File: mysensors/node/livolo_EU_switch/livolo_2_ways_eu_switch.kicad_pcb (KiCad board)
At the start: 2 copper layers, 47 parts, among them CON1 AVR-ISP-6, IC1 ATMEGA328P-A, P1 Sense Pad, P2 Sense Pad, P3 ANTENNA, P4 CONN_02X06, U1 MIC5205-3.3, U2 MCP16301, U3 TTP223, U4 TTP223, U5 RFM69HW

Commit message: mysensors livolo EU switch panel schematic/pcb progress - 2nd pass
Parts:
- removed R9: 1K, Resistors_SMD:R_0603_HandSoldering
- added R1: 31K6, Resistors_SMD:R_0603_HandSoldering, F.Cu at (165.0, 106.9)
- CON1: footprint Pin_Headers:Pin_Header_Straight_SMT_02x03 -> myfootprints:AVR_ISP_SMT_Small_02x03
- D3, D6: value LED_Small -> LED_Blue
- D4, D5: value LED_Small -> LED_Red
- P4: value CONN_02X06 -> Power Board
- R2: value 31K6 -> 10K
- R5: value 10K -> 1K
- U5: value RFM69HW -> RFM69CW; footprint mysensors_radios:RFM69HW_SMD_Handsoldering -> myfootprints:RFM69CW
- moved D5 100.4 mm to (145.4, 106.3)
- moved CON1 95.7 mm to (139.8, 91.9)
- moved L2 95.6 mm to (138.2, 105.1)
- moved R8 91.0 mm to (184.6, 103.6)
- moved R6 89.4 mm to (171.0, 105.3)
- moved C12 89.2 mm to (175.5, 105.3)
- moved D3 87.4 mm to (153.9, 106.3)
- moved C1 87.3 mm to (160.4, 106.9)
- moved D6 84.6 mm to (168.5, 93.1)
- moved R5 83.9 mm to (182.0, 93.6)
- moved P1 82.8 mm to (135.1, 76.2)
- moved U1 81.4 mm to (164.7, 86.5)
- moved U3 77.2 mm to (183.2, 80.2)
- moved D2 77.0 mm to (190.1, 79.3)
- moved U5 76.2 mm to (126.1, 96.4)
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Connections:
- net /D0 renamed Net-(IC1-Pad30)
- D3 pad 1: Net-(D3-Pad1) -> GND
- D4 pad 2: Net-(D4-Pad2) -> +3V3
- D5 pad 2: Net-(D5-Pad2) -> +3V3
- D6 pad 1: Net-(D6-Pad1) -> GND
- IC1 pad 12: Net-(IC1-Pad12) -> /S1_LEDs
- IC1 pad 13: Net-(IC1-Pad13) -> /TS1
- IC1 pad 25: Net-(IC1-Pad25) -> /S2_LEDs
- IC1 pad 28: Net-(IC1-Pad28) -> /TS2
- P1 pad 1: Net-(C11-Pad1) -> Net-(C12-Pad1)
- P2 pad 1: Net-(C12-Pad1) -> Net-(C11-Pad1)
- P4 pad 11: Net-(P4-Pad11) -> /12Vcc
- P4 pad 4: Net-(P4-Pad4) -> GND
- R2 pad 1: Net-(R2-Pad1) -> GND
- R2 pad 2: Net-(C7-Pad1) -> Net-(R1-Pad1)
- R3 pad 1: GND -> +3V3
- R3 pad 2: Net-(R2-Pad1) -> /RESET
- R4 pad 1: +3V3 -> /SS
- R4 pad 2: /RESET -> +3V3
- R5 pad 1: /SS -> Net-(D6-Pad2)
- R5 pad 2: +3V3 -> /S1_LEDs
- R6 pad 1: Net-(R6-Pad1) -> Net-(D5-Pad1)
- R6 pad 2: Net-(R6-Pad2) -> /S1_LEDs
- R7 pad 1: Net-(R7-Pad1) -> Net-(D3-Pad2)
- R7 pad 2: Net-(R7-Pad2) -> /S2_LEDs
- R8 pad 1: Net-(R8-Pad1) -> Net-(D4-Pad1)
- R8 pad 2: Net-(R8-Pad2) -> /S2_LEDs
- U2 pad 3: Net-(R2-Pad1) -> Net-(R1-Pad1)
- U3 pad 1: Net-(U3-Pad1) -> /TS1
- U4 pad 1: Net-(U4-Pad1) -> /TS2
- U5 pad 1: Net-(U5-Pad1) -> Net-(P3-Pad1)
- U5 pad 10: Net-(P3-Pad1) -> Net-(U5-Pad10)
- U5 pad 11: GND -> Net-(U5-Pad11)
- U5 pad 12: /SCK -> Net-(U5-Pad12)
- U5 pad 13: /MISO -> Net-(U5-Pad13)
- U5 pad 14: /MOSI -> GND
- U5 pad 2: /INT -> +3V3
- U5 pad 3: Net-(U5-Pad3) -> GND
- U5 pad 5: Net-(U5-Pad5) -> /MOSI
- U5 pad 6: Net-(U5-Pad6) -> /SCK
- U5 pad 7: Net-(U5-Pad7) -> /SS
- U5 pad 8: +3V3 -> /MISO
- U5 pad 9: GND -> /INT
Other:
- net class Default: clearance 0.2 -> 0.3; trace_width 0.25 -> 0.35
- rule trace_clearance: 0.2 -> 0.3

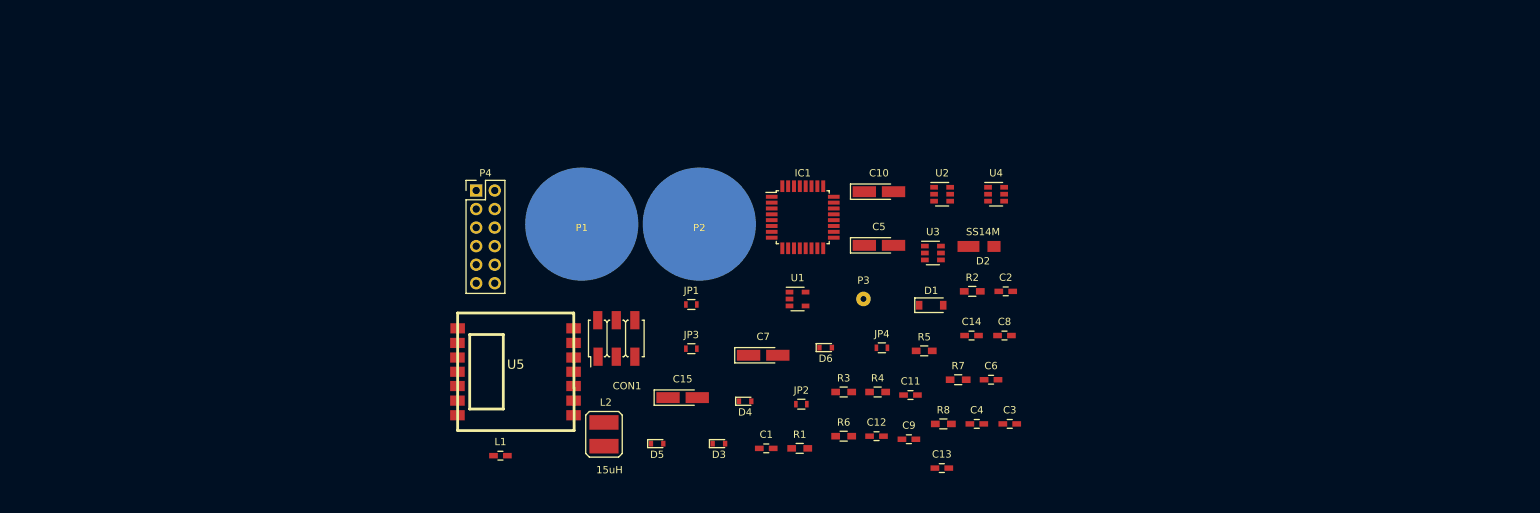
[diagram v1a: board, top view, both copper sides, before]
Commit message: mysensors livolo EU switch panel schematic/pcb progress - 3rd pass
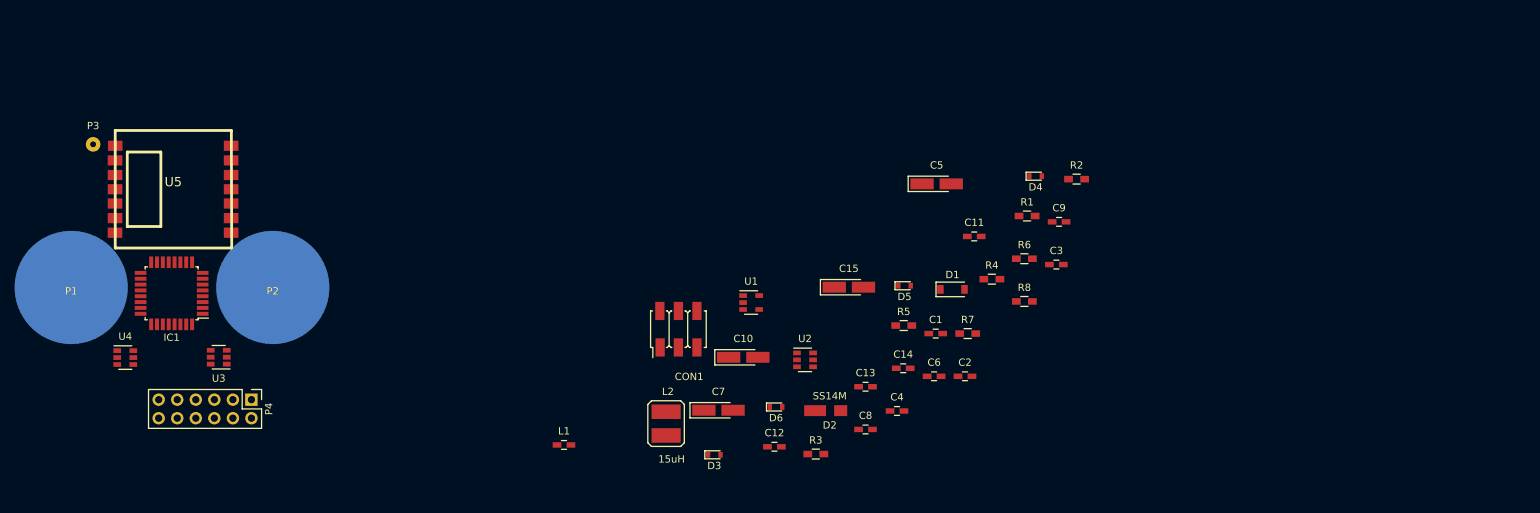
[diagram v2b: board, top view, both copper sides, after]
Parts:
- removed JP1, JP3: Toggle/Direct, Resistors_SMD:R_0603
- removed JP2, JP4: Out_H/L, Resistors_SMD:R_0603
- C11, C12: value 4p7* -> 0-50pf*
- IC1: value ATMEGA328P-A -> ATMEGA328P-AU
- P1: value Sense Pad -> Sense Pad 2
- P2: value Sense Pad -> Sense Pad 1
- moved U4 121.3 mm to (72.6, 94.5)
- moved P3 107.6 mm to (68.2, 65.3)
- moved U3 98.8 mm to (85.4, 94.5), turned to 180 degrees
- moved IC1 87.0 mm to (79.0, 85.7), turned to 180 degrees
- moved P1 70.4 mm to (65.2, 84.9)
- moved P2 59.0 mm to (92.8, 84.9)
- moved U5 53.1 mm to (79.2, 71.5)
- moved D4 50.3 mm to (197.3, 69.7)
- moved R1 44.5 mm to (196.1, 75.1)
- moved P4 42.0 mm to (89.9, 100.3), turned to 270 degrees
- moved D5 40.2 mm to (179.3, 84.7)
- moved C9 36.2 mm to (200.5, 75.9)
- moved R6 34.7 mm to (195.7, 81.0)
- moved D2 30.8 mm to (169.1, 101.8)
- moved U2 29.4 mm to (165.7, 94.8)
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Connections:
- IC1 pad 1: Net-(IC1-Pad1) -> /TS1
- IC1 pad 12: /S1_LEDs -> Net-(IC1-Pad12)
- IC1 pad 13: /TS1 -> Net-(IC1-Pad13)
- IC1 pad 2: Net-(IC1-Pad2) -> /S1_LEDs
- IC1 pad 23: Net-(IC1-Pad23) -> /S2_LEDs
- IC1 pad 24: Net-(IC1-Pad24) -> /TS2
- IC1 pad 25: /S2_LEDs -> Net-(IC1-Pad25)
- IC1 pad 28: /TS2 -> Net-(IC1-Pad28)
- IC1 pad 30: Net-(IC1-Pad30) -> /Relay2
- IC1 pad 31: Net-(IC1-Pad31) -> /Relay1
- P4 pad 10: Net-(P4-Pad10) -> /Relay1
- P4 pad 12: Net-(P4-Pad12) -> /Relay2
- U3 pad 4: Net-(JP2-Pad1) -> +3V3
- U3 pad 6: Net-(JP1-Pad1) -> GND
- U4 pad 4: Net-(JP4-Pad1) -> +3V3
- U4 pad 6: Net-(JP3-Pad1) -> GND
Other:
- net class Default: clearance 0.3 -> 0.2; trace_width 0.35 -> 0.25
- rule trace_clearance: 0.3 -> 0.2

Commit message: mysensors livolo EU switch panel schematic/pcb progress - 4th pass
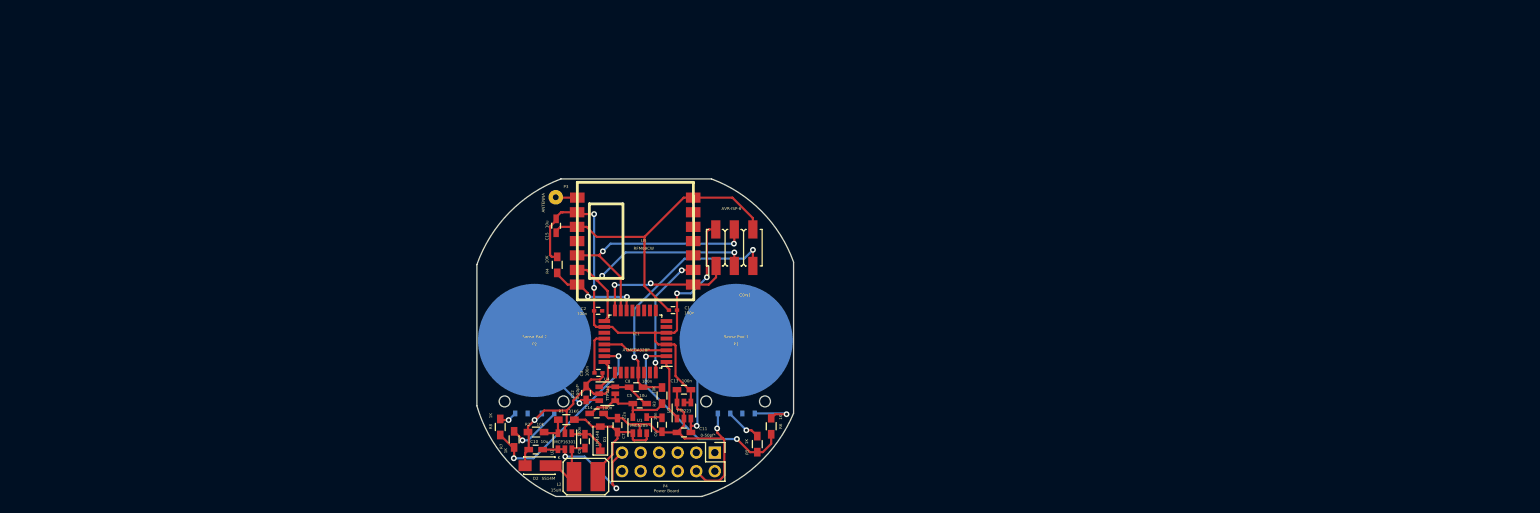
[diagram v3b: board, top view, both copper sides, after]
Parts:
- removed C3: 100n, Capacitors_SMD:C_0603_HandSoldering
- removed L1: BLM18HE152SN1D, Capacitors_SMD:C_0603_HandSoldering
- added REF**: hole_1.5mm, myfootprints:hole_1.5mm, F.Cu at (160.2, 100.5)
- added REF**: hole_1.5mm, myfootprints:hole_1.5mm, F.Cu at (152.2, 100.5)
- added REF**: hole_1.5mm, myfootprints:hole_1.5mm, F.Cu at (124.5, 100.5)
- added REF**: hole_1.5mm, myfootprints:hole_1.5mm, F.Cu at (132.6, 100.5)
- C1, C2, C4: footprint Capacitors_SMD:C_0603_HandSoldering -> Capacitors_SMD:C_0402
- C10, C15, C5, C7: footprint Capacitors_Tantalum_SMD:Tantalum_Case-A_EIA-3216-18_Hand -> Capacitors_SMD:C_0603_HandSoldering
- D3, D6: value LED_Blue -> Blue; moved to B.Cu
- D4, D5: value LED_Red -> Red; moved to B.Cu
- IC1: value ATMEGA328P-AU -> ATMEGA328P
- P1: value Sense Pad 2 -> Sense Pad 1
- P2: value Sense Pad 1 -> Sense Pad 2
- U1: value MIC5205-3.3 -> MIC5205
- moved P1 91.3 mm to (156.2, 92.2)
- moved R2 81.7 mm to (128.8, 104.7)
- moved D4 77.5 mm to (126.8, 102.2)
- moved R8 73.8 mm to (124.0, 104.0), turned to 270 degrees
- moved C9 71.5 mm to (135.6, 106.0), turned to 270 degrees
- moved R1 69.0 mm to (133.0, 103.0)
- moved U4 66.2 mm to (138.6, 99.5)
- moved U3 64.1 mm to (149.1, 101.8), turned to 90 degrees
- moved P4 63.9 mm to (153.3, 107.5)
- moved IC1 63.8 mm to (142.4, 92.3)
- moved REF** 63.8 mm to (142.5, 91.9)
- moved R7 63.8 mm to (125.8, 105.7), turned to 270 degrees
- moved P3 63.8 mm to (131.6, 72.5)
- moved U5 63.7 mm to (142.4, 78.5)
- moved R4 59.6 mm to (131.8, 81.8), turned to 90 degrees
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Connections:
- C15 pad 1: +3V3 -> GND
- C15 pad 2: GND -> +3V3
- C2 pad 2: Net-(C2-Pad2) -> +3V3
- IC1 pad 18: Net-(C2-Pad2) -> +3V3
- P1 pad 1: Net-(C12-Pad1) -> Net-(C11-Pad1)
- P2 pad 1: Net-(C11-Pad1) -> Net-(C12-Pad1)
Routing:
- net GND: track 0.00 -> 128.3 mm, vias 0 -> 2
- net +3V3: track 0.00 -> 85.0 mm, vias 0 -> 4
- net /RESET: track 0.00 -> 35.6 mm, vias 0 -> 2
- net /MOSI: track 0.00 -> 32.9 mm, vias 0 -> 2
- net /SCK: track 0.00 -> 31.9 mm, vias 0 -> 2
- net /S1_LEDs: track 0.00 -> 29.6 mm, vias 0 -> 2
- net /S2_LEDs: track 0.00 -> 27.6 mm, vias 0 -> 2
- net Net-(C7-Pad1): track 0.00 -> 19.7 mm
- net /MISO: track 0.00 -> 19.6 mm, vias 0 -> 2
- net /12Vcc: track 0.00 -> 18.5 mm, vias 0 -> 2
- net /INT: track 0.00 -> 17.1 mm, vias 0 -> 2
- net Net-(C11-Pad1): track 0.00 -> 16.7 mm, vias 0 -> 1
- net Net-(C12-Pad1): track 0.00 -> 14.2 mm, vias 0 -> 1
- net /SS: track 0.00 -> 13.2 mm, vias 0 -> 2
- net Net-(C9-Pad2): track 0.00 -> 9.13 mm
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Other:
- board outline added: 43.4 x 43.5 mm
- net class Default: clearance 0.2 -> 0.3; trace_width 0.25 -> 0.3
- rule trace_clearance: 0.2 -> 0.3
- board text added: "K"

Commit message: mysensors livolo EU switch panel schematic/pcb progress - 5th pass
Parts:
- IC1: value ATMEGA328P -> ATMEGA328P-AU
- U1: value MIC5205 -> MIC5205-3.3
- moved C2 0.60 mm to (137.3, 87.5)
- moved C1 0.51 mm to (147.5, 87.5)
- moved C4 0.39 mm to (137.2, 96.9), turned to 0 degrees
- moved CON1 0.35 mm to (156.3, 79.5)
- moved R1 0.21 mm to (132.9, 103.2)
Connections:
- IC1 pad 27: Net-(IC1-Pad27) -> /Relay1
- IC1 pad 28: Net-(IC1-Pad28) -> /Relay2
- IC1 pad 30: /Relay2 -> Net-(IC1-Pad30)
- IC1 pad 31: /Relay1 -> Net-(IC1-Pad31)
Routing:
- net +3V3: track 85.0 -> 121.5 mm, vias 4 -> 13
- net GND: track 128.3 -> 164.6 mm, vias 2 -> 7
- net /Relay1: track 0.00 -> 23.6 mm, vias 0 -> 1
- net /Relay2: track 0.00 -> 18.5 mm, vias 0 -> 1
- net Net-(D4-Pad1): track 2.48 -> 5.16 mm
- net Net-(C4-Pad2): track 5.90 -> 7.54 mm, vias 0 -> 2
- net /RESET: track 35.6 -> 37.0 mm
- net Net-(D6-Pad2): track 5.04 -> 6.35 mm
- net Net-(D5-Pad1): track 6.72 -> 5.42 mm
- net /S1_LEDs: track 29.6 -> 30.5 mm
- net Net-(C12-Pad1): track 14.2 -> 13.4 mm
- net /INT: track 17.1 -> 17.9 mm
- net /TS1: track 8.35 -> 8.91 mm
- net /MISO: track 19.6 -> 19.0 mm

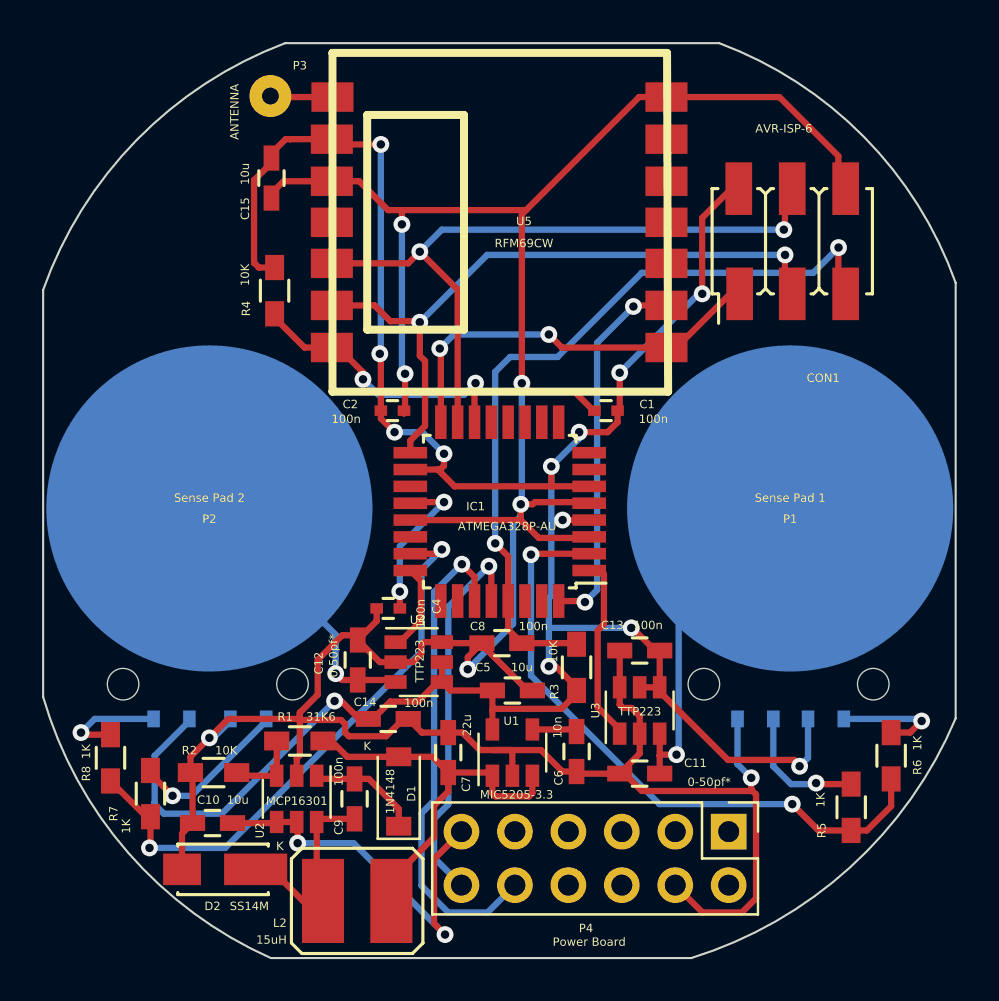
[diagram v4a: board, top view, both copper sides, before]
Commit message: mysensors livolo EU switch panel schematic/pcb progress - 6th pass
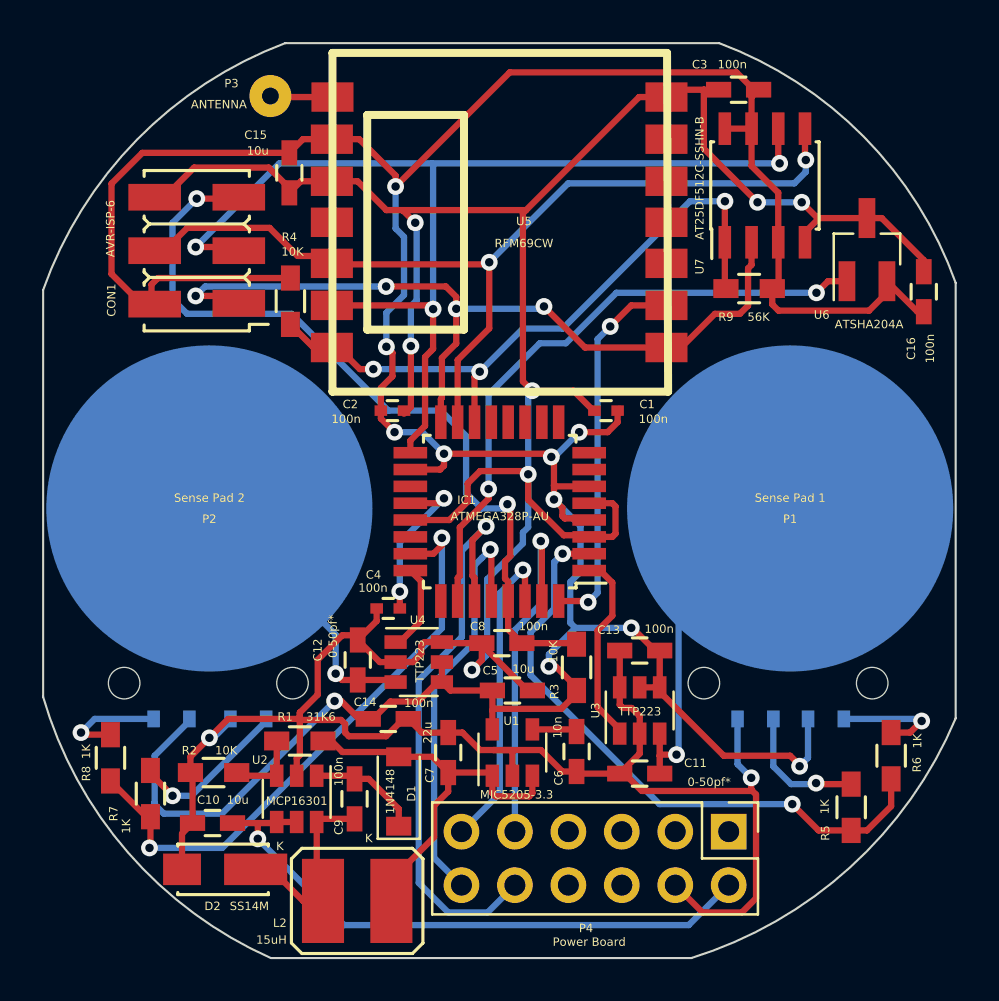
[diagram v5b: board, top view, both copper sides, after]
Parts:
- removed the REF** at (160.2, 100.5)
- removed the REF** at (152.2, 100.5)
- removed the REF** at (124.5, 100.5)
- removed the REF** at (132.6, 100.5)
- added C16: 100n, Capacitors_SMD:C_0603_HandSoldering, F.Cu at (162.6, 81.8)
- added C3: 100n, Capacitors_SMD:C_0603_HandSoldering, F.Cu at (153.8, 72.2)
- added R9: 56K, Resistors_SMD:R_0603_HandSoldering, F.Cu at (154.3, 81.7)
- added REF**: hole_1.5mm, myfootprints:hole_1.5mm, F.Cu at (152.2, 100.5)
- added REF**: hole_1.5mm, myfootprints:hole_1.5mm, F.Cu at (160.2, 100.5)
- added REF**: hole_1.5mm, myfootprints:hole_1.5mm, F.Cu at (132.6, 100.5)
- added REF**: hole_1.5mm, myfootprints:hole_1.5mm, F.Cu at (124.6, 100.5)
- added U6: AT25DF512C-SSHN-B, Housings_SOIC:SOIC-8_3.9x4.9mm_Pitch1.27mm, F.Cu at (155.1, 76.8)
- added U7: ATSHA204A, TO_SOT_Packages_SMD:SOT-23_Handsoldering, F.Cu at (159.9, 79.8)
- moved CON1 28.3 mm to (128.1, 79.9), turned to 90 degrees
- moved R4 0.90 mm to (132.5, 82.3)
- moved C15 0.89 mm to (132.4, 76.2)
- moved REF** 0.05 mm to (142.5, 91.8)
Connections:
- net /Relay1 renamed /Relay1_Set
- net /Relay2 renamed /Relay2_Set
- IC1 pad 10: Net-(IC1-Pad10) -> (no net)
- IC1 pad 11: Net-(IC1-Pad11) -> (no net)
- IC1 pad 12: Net-(IC1-Pad12) -> (no net)
- IC1 pad 13: Net-(IC1-Pad13) -> (no net)
- IC1 pad 19: Net-(IC1-Pad19) -> (no net)
- IC1 pad 22: Net-(IC1-Pad22) -> (no net)
- IC1 pad 25: Net-(IC1-Pad25) -> (no net)
- IC1 pad 26: Net-(IC1-Pad26) -> /ATSHA204A
- IC1 pad 30: Net-(IC1-Pad30) -> /Relay2_Reset
- IC1 pad 31: Net-(IC1-Pad31) -> /Relay1_Reset
- IC1 pad 7: Net-(IC1-Pad7) -> (no net)
- IC1 pad 8: Net-(IC1-Pad8) -> (no net)
- IC1 pad 9: Net-(IC1-Pad9) -> (no net)
- P4 pad 1: Net-(P4-Pad1) -> (no net)
- P4 pad 11: /12Vcc -> /Relay2_Reset
- P4 pad 2: Net-(P4-Pad2) -> /12Vcc
- P4 pad 3: Net-(P4-Pad3) -> (no net)
- P4 pad 5: Net-(P4-Pad5) -> (no net)
- P4 pad 6: Net-(P4-Pad6) -> (no net)
- P4 pad 7: Net-(P4-Pad7) -> (no net)
- P4 pad 8: Net-(P4-Pad8) -> (no net)
- P4 pad 9: Net-(P4-Pad9) -> /Relay1_Reset
- U5 pad 10: Net-(U5-Pad10) -> (no net)
- U5 pad 11: Net-(U5-Pad11) -> (no net)
- U5 pad 12: Net-(U5-Pad12) -> (no net)
- U5 pad 13: Net-(U5-Pad13) -> (no net)
- U5 pad 4: Net-(U5-Pad4) -> (no net)
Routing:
- net +3V3: track 121.5 -> 166.7 mm, vias 13 -> 11
- net /ATSHA204A: track 0.00 -> 29.7 mm, vias 0 -> 2
- net /MISO: track 19.0 -> 39.7 mm, vias 2 -> 4
- net /SCK: track 31.6 -> 52.1 mm, vias 2 -> 3
- net GND: track 164.6 -> 183.9 mm, vias 7 -> 9
- net /SS: track 13.6 -> 31.6 mm, vias 2 -> 3
- net /Relay1_Reset: track 0.00 -> 17.2 mm, vias 0 -> 1
- net /Relay2_Reset: track 0.00 -> 15.2 mm, vias 0 -> 1
- net /MOSI: track 33.0 -> 44.4 mm
- net /12Vcc: track 18.5 -> 28.7 mm, vias 2 -> 1
- net /Relay1_Set: track 23.6 -> 27.8 mm
- net /Relay2_Set: track 18.5 -> 20.1 mm
- net /RESET: track 37.0 -> 38.6 mm
- net /S2_LEDs: track 27.7 -> 28.6 mm
- net /S1_LEDs: track 30.5 -> 29.6 mm
